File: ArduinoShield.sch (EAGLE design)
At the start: 10 parts

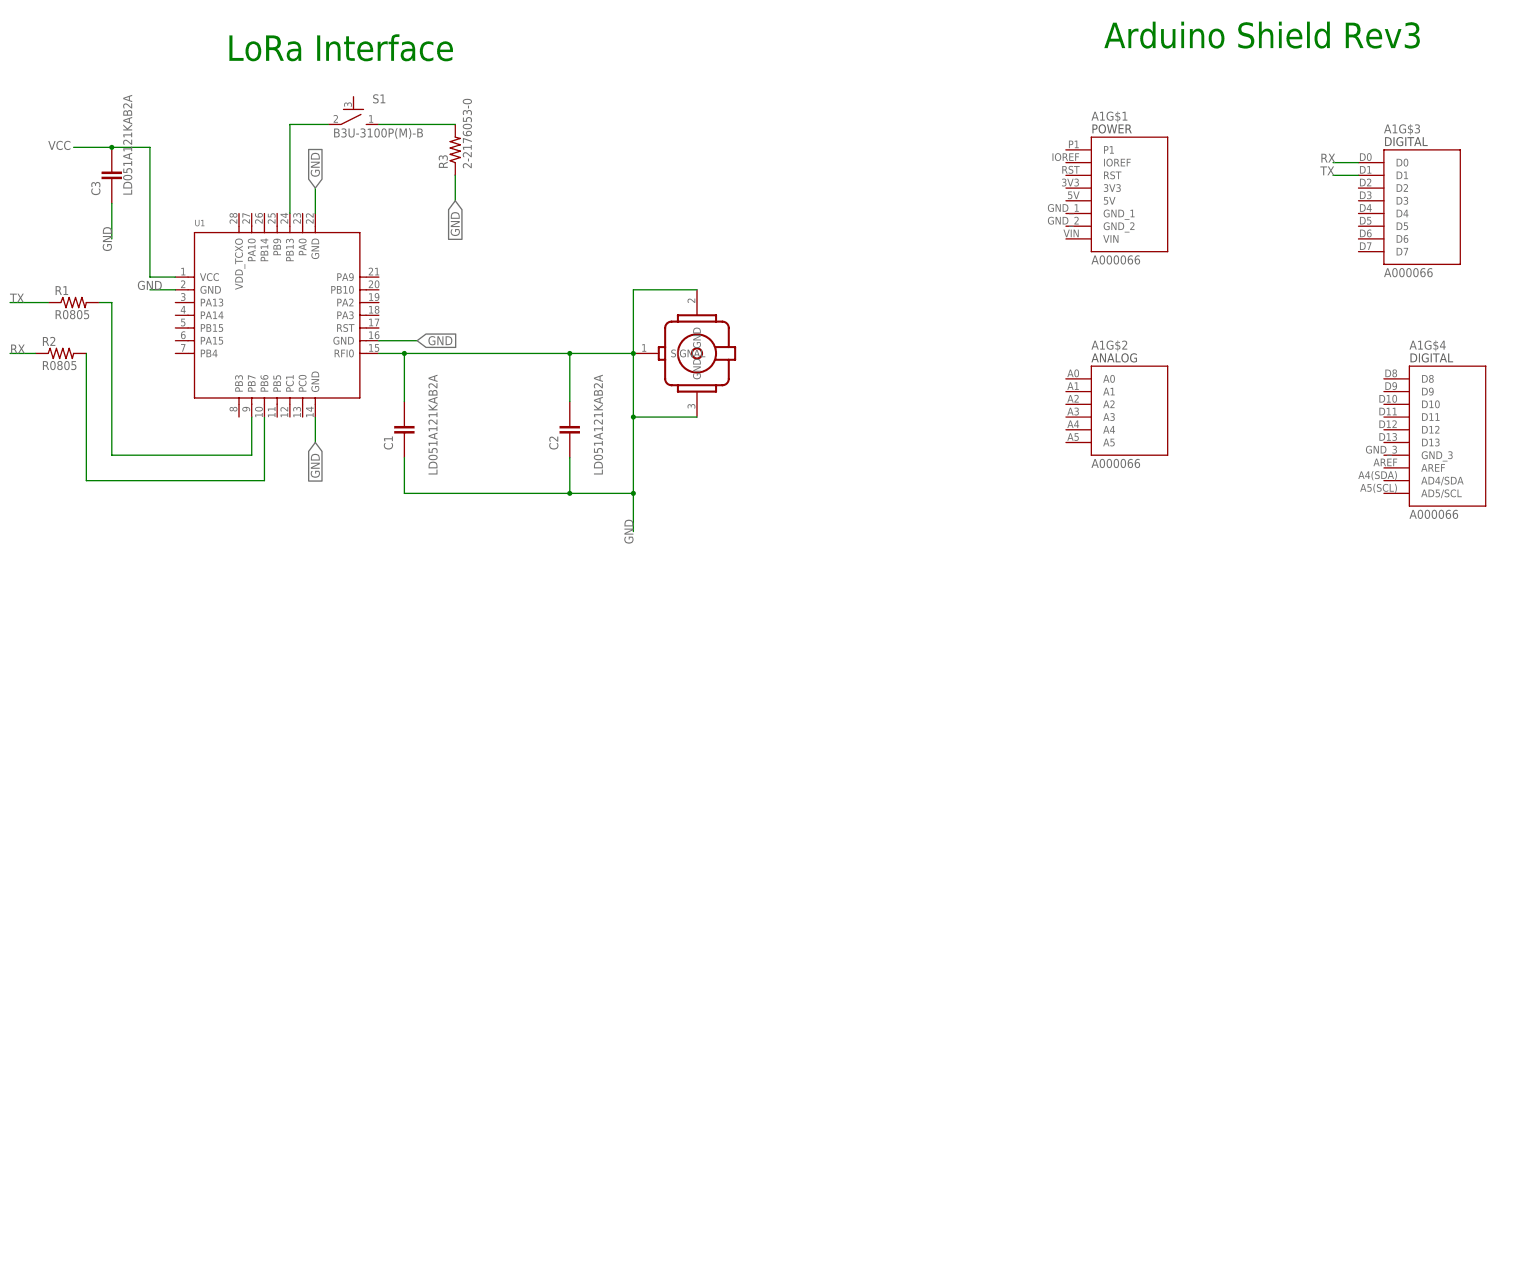
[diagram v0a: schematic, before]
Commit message: Stubbed in lora
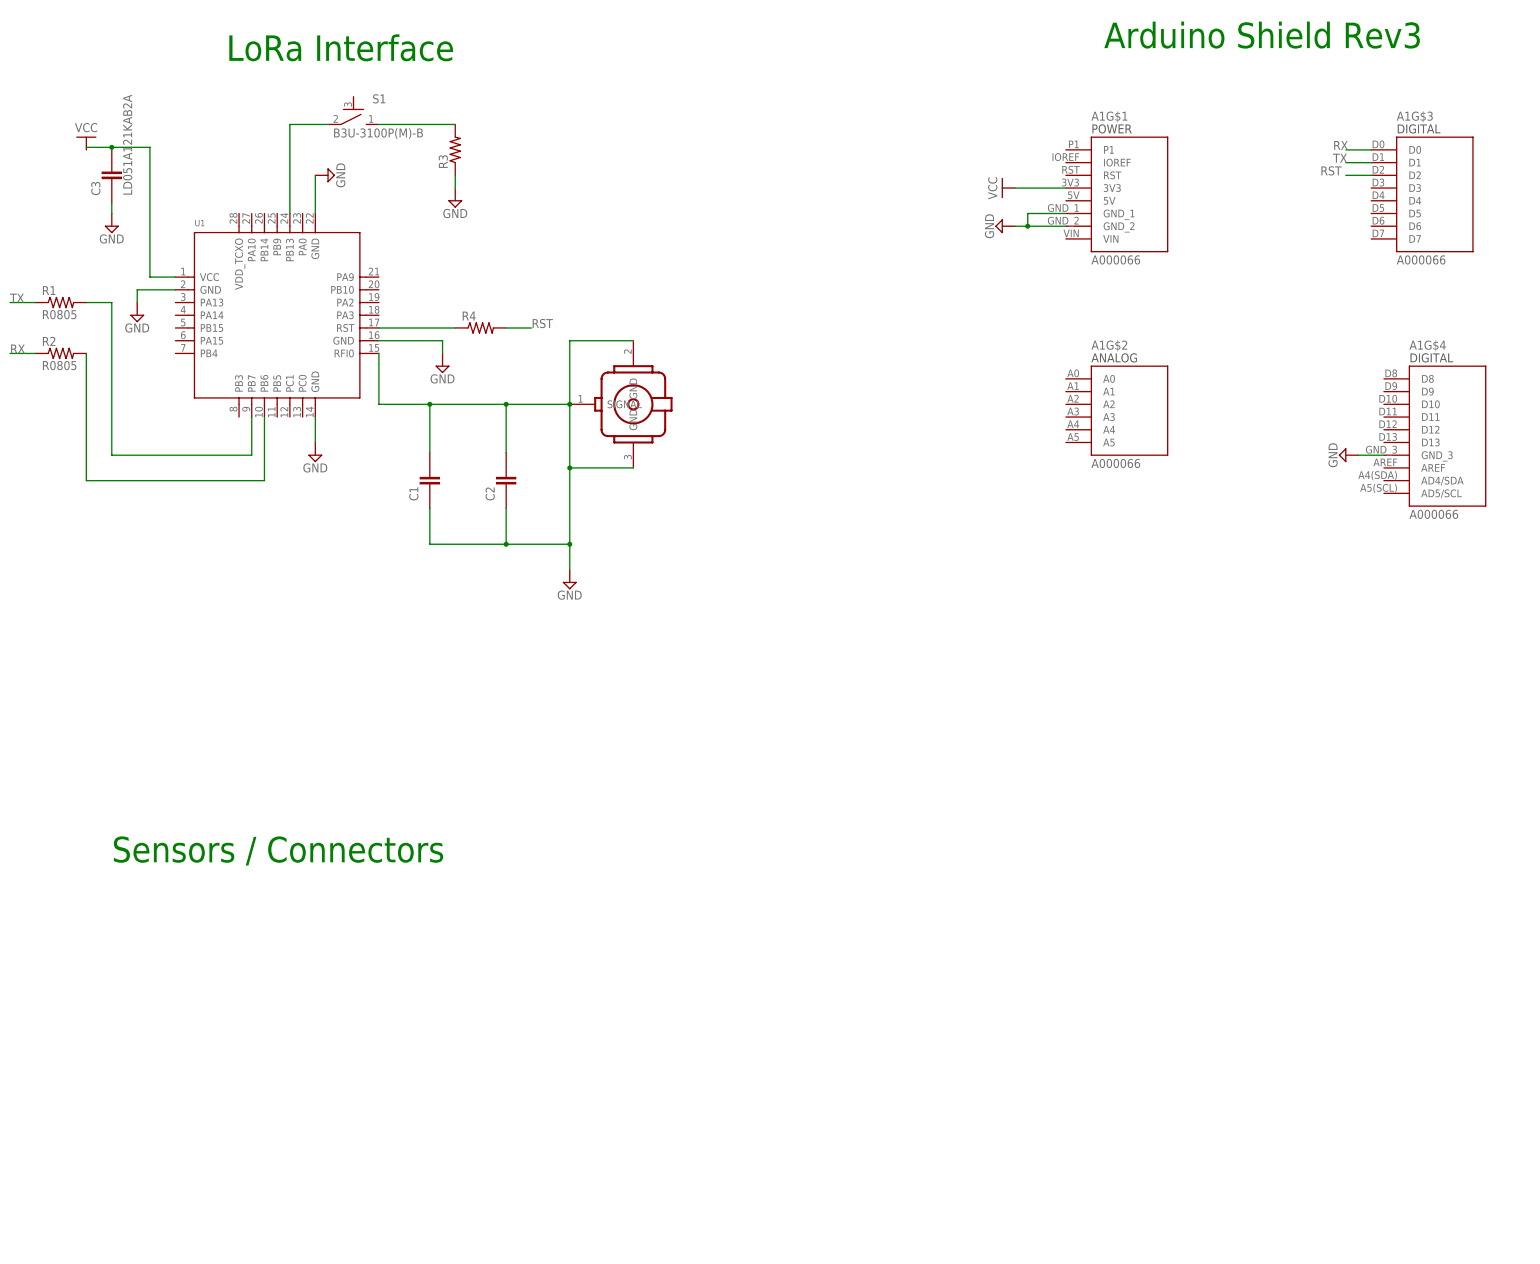
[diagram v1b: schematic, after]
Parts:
- added R4: 2-2176053-0, R0805:2-2176053-0
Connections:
- new net N$4: C3.1
- new net N$5: R4.1, U1.RST
- new net RST: A1G$3.D2, R4.2
- net GND: now also A1G$1.GND_1, A1G$1.GND_2, A1G$4.GND_3; no longer C3.1
- net VCC: now also A1G$1.3V3
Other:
- note added: "Sensors / Connectors"
- moved on the sheet: A1G$3, C1, C2, R1

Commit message: stubbed in i2c
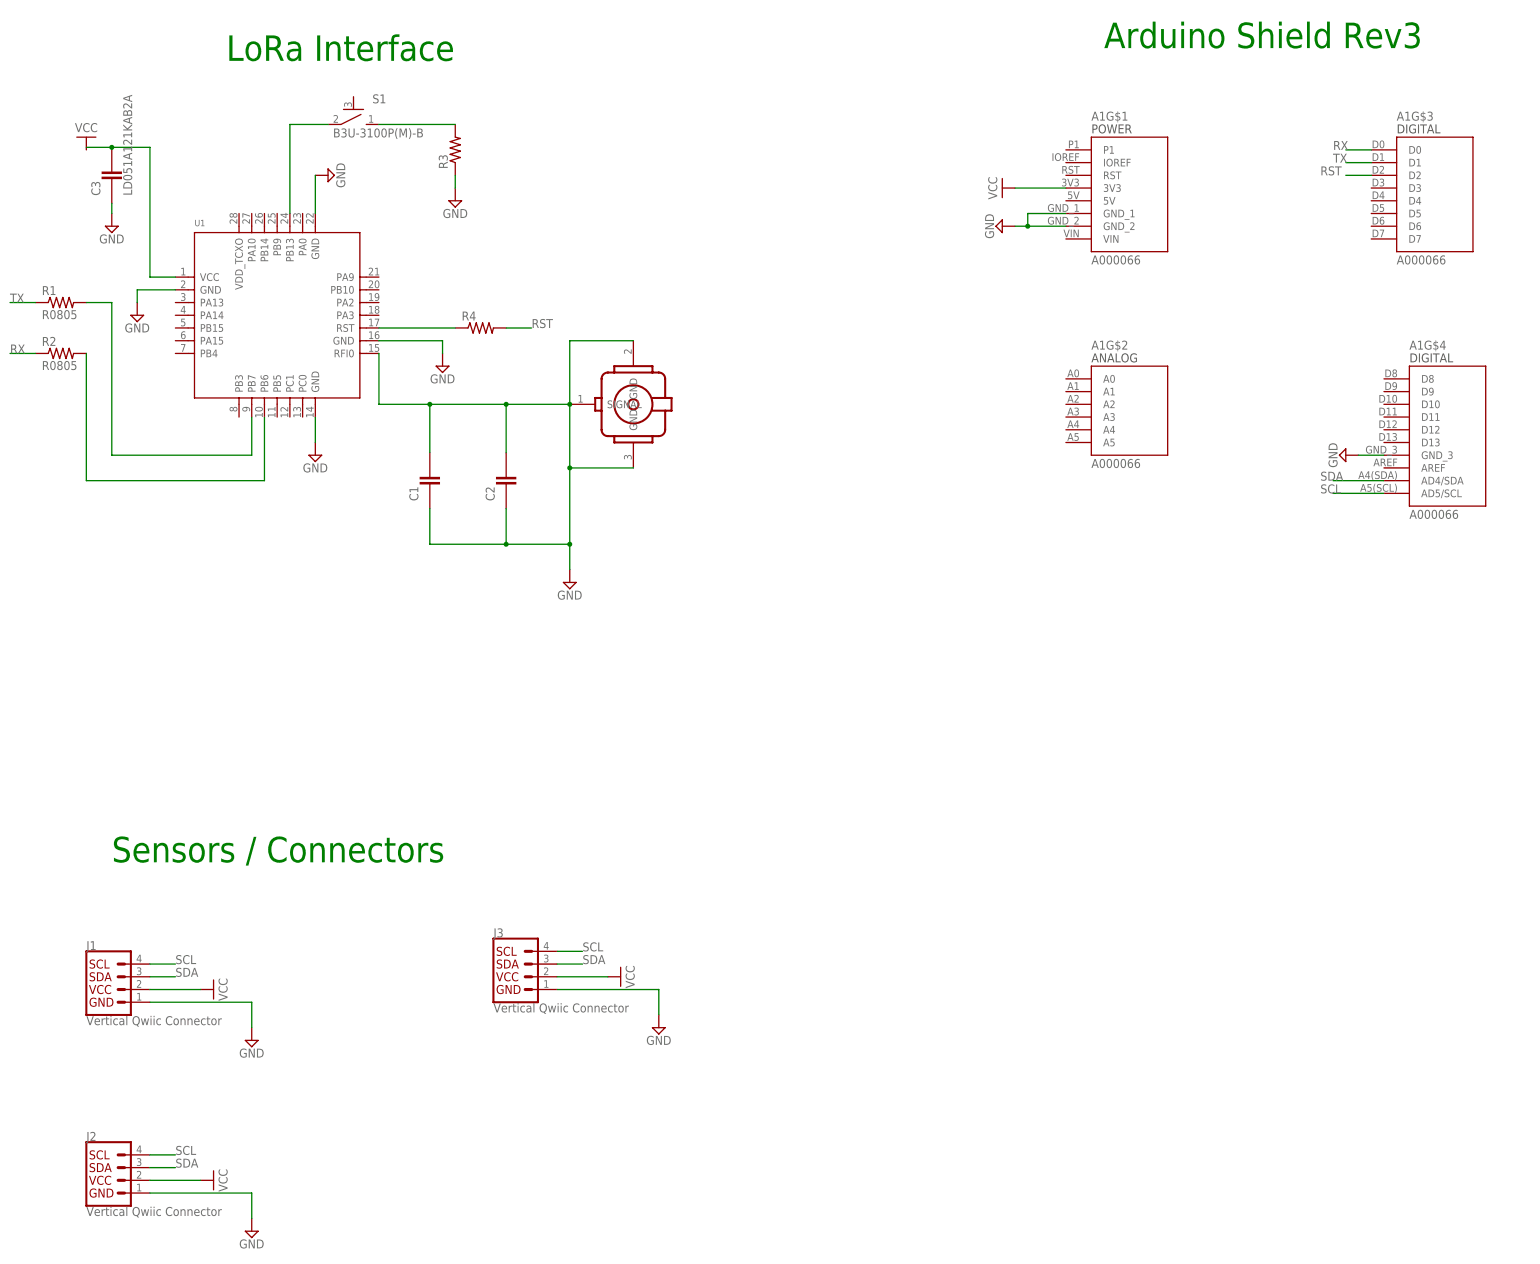
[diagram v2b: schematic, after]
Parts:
- added J1, J2, J3: Vertical Qwiic Connector, SparkFun-Connectors:QWIIC_CONNECTOR
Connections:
- new net SCL: A1G$4.AD5/SCL, J1.4, J2.4, J3.4
- new net SDA: A1G$4.AD4/SDA, J1.3, J2.3, J3.3
- net GND: now also J1.1, J2.1, J3.1
- net VCC: now also J1.2, J2.2, J3.2
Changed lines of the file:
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@@
 <layer number="56" name="wert" color="7" fill="1" visible="no" active="no"/>
 <layer number="57" name="tCAD" color="7" fill="1" visible="no" active="no"/>
+<layer number="58" name="bCAD" color="7" fill="1" visible="no" active="no"/>
 <layer number="59" name="tCarbon" color="7" fill="1" visible="no" active="no"/>
 <layer number="60" name="bCarbon" color="7" fill="1" visible="no" active="no"/>
@@
 <layer number="156" name="DXF0409-TOP" color="7" fill="1" visible="no" active="no"/>
 <layer number="157" name="DXF0409-BOTTOM" color="7" fill="1" visible="no" active="no"/>
+<layer number="158" name="FaceMMeas" color="7" fill="1" visible="no" active="no"/>
+<layer number="159" name="Geh-Bear2" color="7" fill="1" visible="no" active="no"/>
+<layer number="160" name="Topologie" color="7" fill="1" visible="no" active="no"/>
+<layer number="161" name="tomplace2" color="7" fill="1" visible="no" active="no"/>
 <layer number="166" name="AntennaArea" color="7" fill="1" visible="no" active="no"/>
 <layer number="168" name="4mmHeightArea" color="7" fill="1" visible="no" active="no"/>
@@
 <layer number="250" name="Descript" color="7" fill="1" visible="no" active="no"/>
 <layer number="251" name="SMDround" color="7" fill="11" visible="no" active="no"/>
+<layer number="252" name="BR-BS" color="7" fill="1" visible="no" active="no"/>
+<layer number="253" name="Extra" color="7" fill="1" visible="no" active="no"/>
 <layer number="254" name="cooling" color="7" fill="1" visible="no" active="yes"/>
 <layer number="255" name="Accent" color="7" fill="1" visible="no" active="no"/>
@@
 <part name="SUPPLY11" library="Power_Symbols" deviceset="GND" device="" value="GND"/>
 <part name="SUPPLY1" library="Power_Symbols" deviceset="GND" device="" value="GND"/>
+<part name="J1" library="SparkFun-Connectors" deviceset="QWIIC_CONNECTOR" device="" value="Vertical Qwiic Connector"/>
+<part name="SUPPLY12" library="Power_Symbols" deviceset="VCC" device="" value="VCC"/>
+<part name="SUPPLY13" library="Power_Symbols" deviceset="GND" device="" value="GND"/>
+<part name="J2" library="SparkFun-Connectors" deviceset="QWIIC_CONNECTOR" device="" value="Vertical Qwiic Connector"/>
+<part name="SUPPLY14" library="Power_Symbols" deviceset="VCC" device="" value="VCC"/>
+<part name="SUPPLY15" library="Power_Symbols" deviceset="GND" device="" value="GND"/>
+<part name="J3" library="SparkFun-Connectors" deviceset="QWIIC_CONNECTOR" device="" value="Vertical Qwiic Connector"/>
+<part name="SUPPLY16" library="Power_Symbols" deviceset="VCC" device="" value="VCC"/>
+<part name="SUPPLY17" library="Power_Symbols" deviceset="GND" device="" value="GND"/>
 </parts>
 <sheets>
@@
 <instance part="SUPPLY1" gate="G$1" x="17.78" y="-40.64" smashed="yes">
 <attribute name="VALUE" x="17.78" y="-43.18" size="1.778" layer="96" align="center"/>
+</instance>
+<instance part="J1" gate="G$1" x="-73.66" y="-121.92" smashed="yes">
+<attribute name="VALUE" x="-78.74" y="-127.254" size="1.778" layer="96" font="vector" align="top-left"/>
+<attribute name="NAME" x="-78.74" y="-114.046" size="1.778" layer="95" font="vector"/>
+</instance>
+<instance part="SUPPLY12" gate="G$1" x="-55.88" y="-121.92" smashed="yes" rot="R270">
+<attribute name="VALUE" x="-51.435" y="-121.92" size="1.778" layer="96" rot="R90" align="center"/>
+</instance>
+<instance part="SUPPLY13" gate="G$1" x="-45.72" y="-132.08" smashed="yes">
+<attribute name="VALUE" x="-45.72" y="-134.62" size="1.778" layer="96" align="center"/>
+</instance>
+<instance part="J2" gate="G$1" x="-73.66" y="-160.02" smashed="yes">
+<attribute name="VALUE" x="-78.74" y="-165.354" size="1.778" layer="96" font="vector" align="top-left"/>
+<attribute name="NAME" x="-78.74" y="-152.146" size="1.778" layer="95" font="vector"/>
+</instance>
+<instance part="SUPPLY14" gate="G$1" x="-55.88" y="-160.02" smashed="yes" rot="R270">
+<attribute name="VALUE" x="-51.435" y="-160.02" size="1.778" layer="96" rot="R90" align="center"/>
+</instance>
+<instance part="SUPPLY15" gate="G$1" x="-45.72" y="-170.18" smashed="yes">
+<attribute name="VALUE" x="-45.72" y="-172.72" size="1.778" layer="96" align="center"/>
+</instance>
+<instance part="J3" gate="G$1" x="7.62" y="-119.38" smashed="yes">
+<attribute name="VALUE" x="2.54" y="-124.714" size="1.778" layer="96" font="vector" align="top-left"/>
+<attribute name="NAME" x="2.54" y="-111.506" size="1.778" layer="95" font="vector"/>
+</instance>
+<instance part="SUPPLY16" gate="G$1" x="25.4" y="-119.38" smashed="yes" rot="R270">
+<attribute name="VALUE" x="29.845" y="-119.38" size="1.778" layer="96" rot="R90" align="center"/>
+</instance>
+<instance part="SUPPLY17" gate="G$1" x="35.56" y="-129.54" smashed="yes">
+<attribute name="VALUE" x="35.56" y="-132.08" size="1.778" layer="96" align="center"/>
 </instance>
 </instances>
@@
 <junction x="5.08" y="-33.02"/>
 </segment>
+<segment>
+<wire x1="-66.04" y1="-124.46" x2="-45.72" y2="-124.46" width="0.1524" layer="91"/>
+<wire x1="-45.72" y1="-124.46" x2="-45.72" y2="-129.54" width="0.1524" layer="91"/>
+<pinref part="SUPPLY13" gate="G$1" pin="GND"/>
+<pinref part="J1" gate="G$1" pin="1"/>
+</segment>
+<segment>
+<wire x1="-66.04" y1="-162.56" x2="-45.72" y2="-162.56" width="0.1524" layer="91"/>
+<wire x1="-45.72" y1="-162.56" x2="-45.72" y2="-167.64" width="0.1524" layer="91"/>
+<pinref part="SUPPLY15" gate="G$1" pin="GND"/>
+<pinref part="J2" gate="G$1" pin="1"/>
+</segment>
+<segment>
+<wire x1="15.24" y1="-121.92" x2="35.56" y2="-121.92" width="0.1524" layer="91"/>
+<wire x1="35.56" y1="-121.92" x2="35.56" y2="-127" width="0.1524" layer="91"/>
+<pinref part="SUPPLY17" gate="G$1" pin="GND"/>
+<pinref part="J3" gate="G$1" pin="1"/>
+</segment>
 </net>
 <net name="N$1" class="0">
@@
 <pinref part="A1" gate="G$1" pin="3V3"/>
 </segment>
+<segment>
+<pinref part="SUPPLY12" gate="G$1" pin="VCC"/>
+<wire x1="-55.88" y1="-121.92" x2="-66.04" y2="-121.92" width="0.1524" layer="91"/>
+<pinref part="J1" gate="G$1" pin="2"/>
+</segment>
+<segment>
+<pinref part="SUPPLY14" gate="G$1" pin="VCC"/>
+<wire x1="-55.88" y1="-160.02" x2="-66.04" y2="-160.02" width="0.1524" layer="91"/>
+<pinref part="J2" gate="G$1" pin="2"/>
+</segment>
+<segment>
+<pinref part="SUPPLY16" gate="G$1" pin="VCC"/>
+<wire x1="25.4" y1="-119.38" x2="15.24" y2="-119.38" width="0.1524" layer="91"/>
+<pinref part="J3" gate="G$1" pin="2"/>
+</segment>
 </net>
 <net name="RX" class="0">
@@
 </segment>
 </net>
+<net name="SDA" class="0">
+<segment>
+<pinref part="A1" gate="G$4" pin="AD4/SDA"/>
+<wire x1="180.34" y1="-20.32" x2="170.18" y2="-20.32" width="0.1524" layer="91"/>
+<label x="167.64" y="-20.32" size="1.778" layer="95"/>
+</segment>
+<segment>
+<pinref part="J1" gate="G$1" pin="3"/>
+<wire x1="-66.04" y1="-119.38" x2="-60.96" y2="-119.38" width="0.1524" layer="91"/>
+<label x="-60.96" y="-119.38" size="1.778" layer="95"/>
+</segment>
+<segment>
+<pinref part="J2" gate="G$1" pin="3"/>
+<wire x1="-66.04" y1="-157.48" x2="-60.96" y2="-157.48" width="0.1524" layer="91"/>
+<label x="-60.96" y="-157.48" size="1.778" layer="95"/>
+</segment>
+<segment>
+<pinref part="J3" gate="G$1" pin="3"/>
+<wire x1="15.24" y1="-116.84" x2="20.32" y2="-116.84" width="0.1524" layer="91"/>
+<label x="20.32" y="-116.84" size="1.778" layer="95"/>
+</segment>
+</net>
+<net name="SCL" class="0">
+<segment>
+<pinref part="A1" gate="G$4" pin="AD5/SCL"/>
+<wire x1="180.34" y1="-22.86" x2="170.18" y2="-22.86" width="0.1524" layer="91"/>
+<label x="167.64" y="-22.86" size="1.778" layer="95"/>
+</segment>
+<segment>
+<pinref part="J1" gate="G$1" pin="4"/>
+<wire x1="-66.04" y1="-116.84" x2="-60.96" y2="-116.84" width="0.1524" layer="91"/>
+<label x="-60.96" y="-116.84" size="1.778" layer="95"/>
+</segment>
+<segment>
+<pinref part="J2" gate="G$1" pin="4"/>
+<wire x1="-66.04" y1="-154.94" x2="-60.96" y2="-154.94" width="0.1524" layer="91"/>
+<label x="-60.96" y="-154.94" size="1.778" layer="95"/>
+</segment>
+<segment>
+<pinref part="J3" gate="G$1" pin="4"/>
+<wire x1="15.24" y1="-114.3" x2="20.32" y2="-114.3" width="0.1524" layer="91"/>
+<label x="20.32" y="-114.3" size="1.778" layer="95"/>
+</segment>
+</net>
